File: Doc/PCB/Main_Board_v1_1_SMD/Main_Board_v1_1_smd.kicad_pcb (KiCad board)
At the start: 2 copper layers, 180 x 98 mm, 138 parts, among them J1 TE_3.5mm_Screwless_P2, J10 BPM, J11 UART, J12 I2C Interface LCD_C, J13 BUZZER_C, J16 IP, J17 -, J19 EP, J2 TE_3.5mm_Screwless_P2, J20 +, J21 VOL_MIN, J22 VOL, J23 VOL_MAX, J24 Conn_01x08, J25 POWEROFF, J26 PMAX, J3 UART_M, J4 Conn_01x08, J5 BUZZER, J6 I2C Interface LCD_M, J7 TE_3.5mm_Screwless_P2, J8 SV2, J9 SV3, Q1 FDT1600N10ALZ, Q2 FDT1600N10ALZ, Q3 FDT1600N10ALZ, Q4 BSR19A, Q5 BSR19A, SW1 MUTE, SW10 BREATH, SW11 EP, SW12 +, SW2 HIST, SW3 VOL_MIN, SW4 VOL, SW5 PBM, SW6 IP, SW7 -, SW8 VOL_MAX, SW9 PMAX, U1 LM358, U2 LM78M05_TO252, U3 XPRESS-40, U4 LM78M05_TO252, U5 XPRESS-40, U6 LCD, U7 LCD

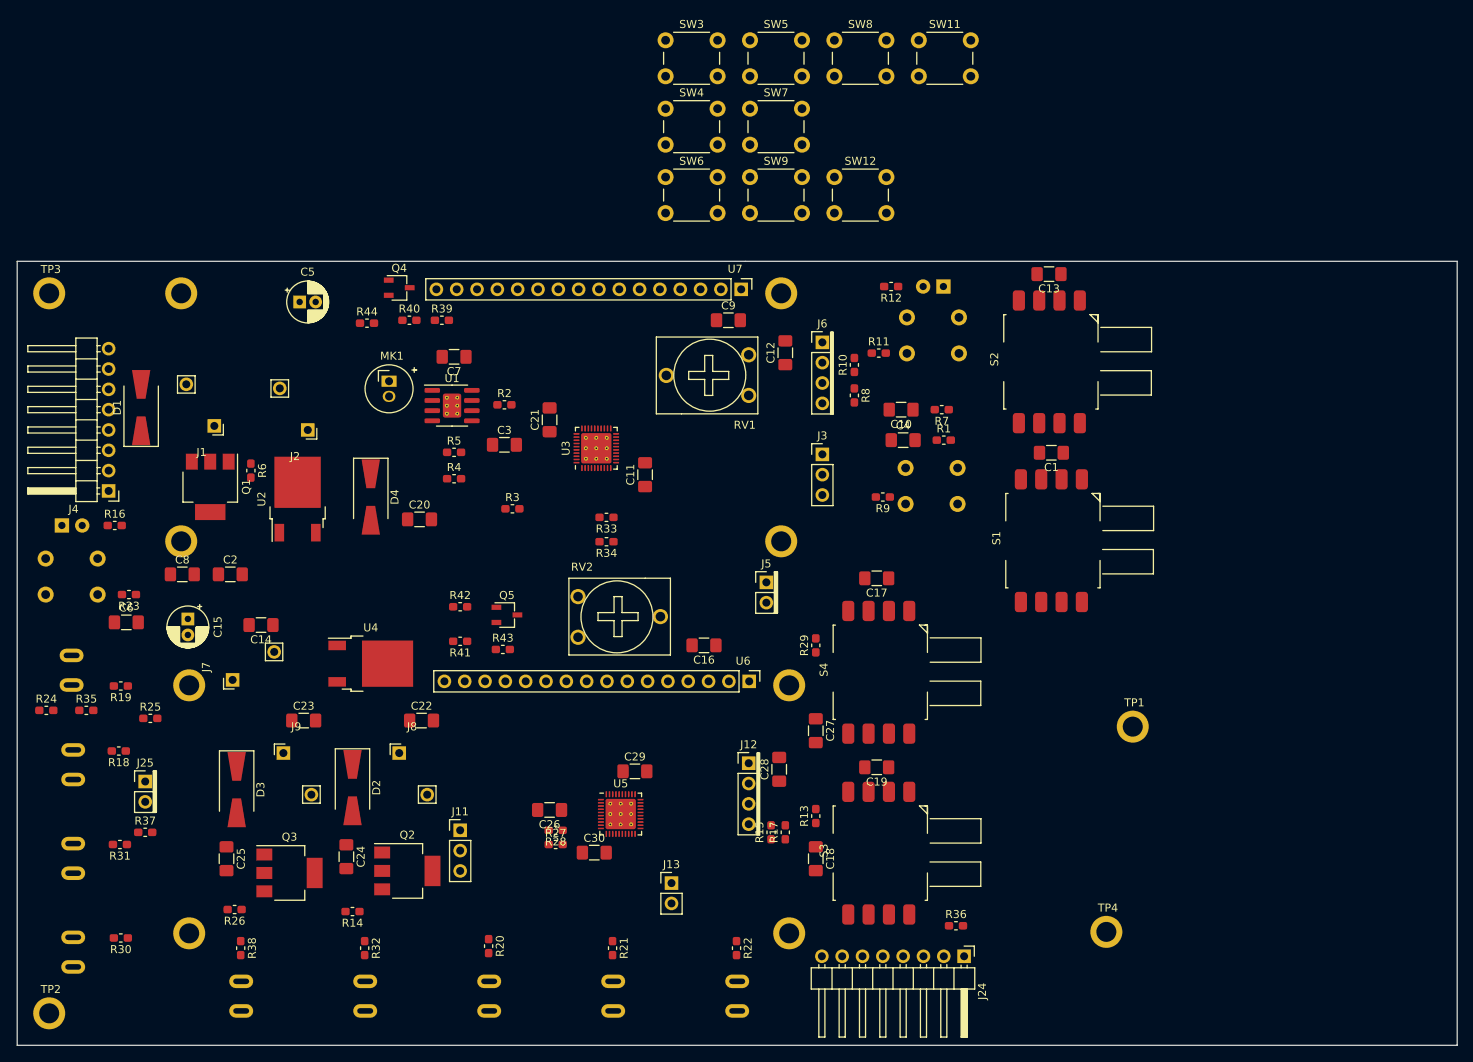
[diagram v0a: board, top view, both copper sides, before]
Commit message: First tests with artificial lung. 70 cases. New PCB THT fixing mounting issues
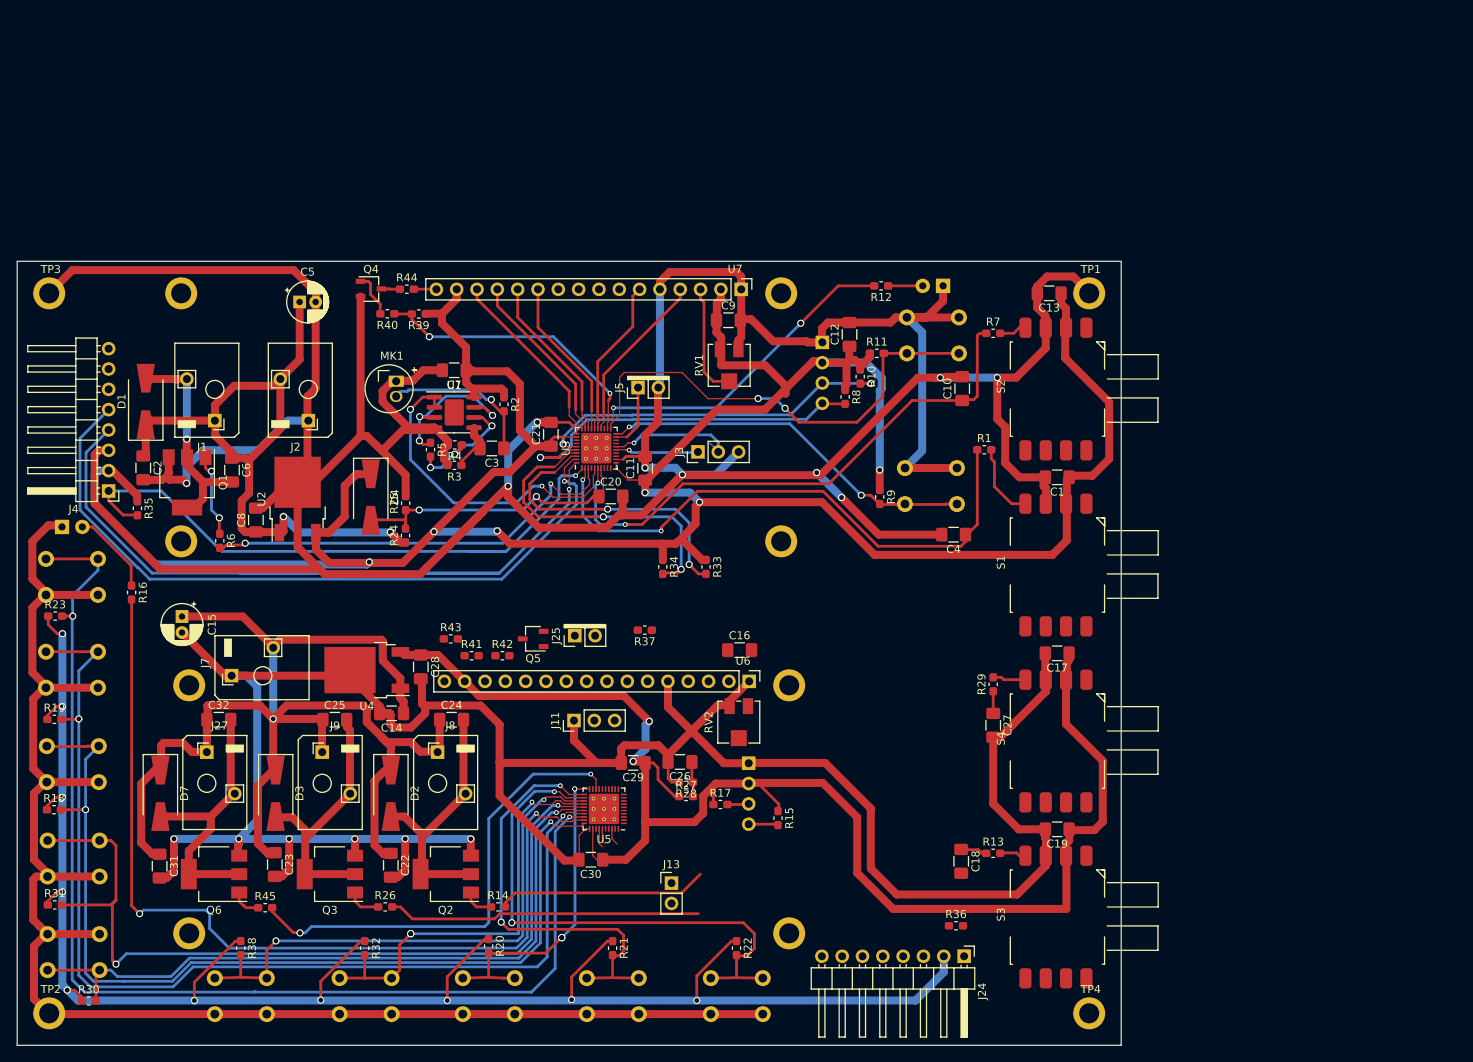
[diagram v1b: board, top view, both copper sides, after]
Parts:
- removed J10: BPM, Ventilator:PushButton
- removed J16: IP, Ventilator:PushButton
- removed J17: -, Ventilator:PushButton
- removed J19: EP, Ventilator:PushButton
- removed J20: +, Ventilator:PushButton
- removed J21: VOL_MIN, Ventilator:PushButton
- removed J22: VOL, Ventilator:PushButton
- removed J23: VOL_MAX, Ventilator:PushButton
- removed J26: PMAX, Ventilator:PushButton
- added C31: 1uF, Capacitor_SMD:C_1206_3216Metric_Pad1.42x1.75mm_HandSolder, F.Cu at (45.2, 108.5)
- added C32: 1uF, Capacitor_SMD:C_1206_3216Metric_Pad1.42x1.75mm_HandSolder, F.Cu at (52.6, 90.2)
- added D7: 1A - 100V, Diode_SMD:D_SMA-SMB_Universal_Handsoldering, F.Cu at (45.3, 99.4)
- added J27: SV2, Ventilator:PinHeader_1x02_Screwless_3.5mm, F.Cu at (51.1, 94.2)
- added Q6: FDT1600N10ALZ, Package_TO_SOT_SMD:SOT-223-3_TabPin2, F.Cu at (52.0, 109.5)
- added R45: 1k, Resistor_SMD:R_0603_1608Metric_Pad1.05x0.95mm_HandSolder, F.Cu at (58.4, 113.7)
- D5: value LED -> ALARM
- J12, J6, SW11, SW12, SW3, SW4, SW6, SW7, SW8, SW9: moved to B.Cu
- R43, R44: value 4.7 -> 1k
- RV1, RV2: value 1K -> 5K; footprint Ventilator:Potentiometer_409HA -> Potentiometer_SMD:Potentiometer_Vishay_TS53YJ_Vertical
- SW5: value PBM -> BPM; moved to B.Cu
- U1: footprint Package_SO:SOIC-8-1EP_3.9x4.9mm_P1.27mm_EP2.29x3mm_ThermalVias -> Package_SO:SOIC-8-1EP_3.9x4.9mm_P1.27mm_EP2.41x3.3mm
- moved SW3 139.6 mm to (31.2, 121.5)
- moved SW8 135.8 mm to (37.7, 105.3), turned to 180 degrees
- moved SW11 122.3 mm to (105.1, 122.5), turned to 180 degrees
- moved SW5 117.2 mm to (120.6, 122.5), turned to 180 degrees
- moved SW9 116.9 mm to (58.6, 122.5), turned to 180 degrees
- moved SW4 113.9 mm to (74.2, 122.5), turned to 180 degrees
- moved SW7 113.9 mm to (37.6, 93.5), turned to 180 degrees
- moved SW12 109.5 mm to (37.5, 81.7), turned to 180 degrees
- moved SW6 101.9 mm to (89.6, 122.5), turned to 180 degrees
- moved R37 67.4 mm to (105.8, 79.0), turned to 180 degrees
- moved J25 56.7 mm to (97.1, 79.7), turned to 90 degrees
- moved TP1 54.4 mm to (161.4, 36.9)
- moved R24 49.9 mm to (75.9, 67.1), turned to 90 degrees
- moved C28 46.6 mm to (77.8, 83.6), turned to 270 degrees
- moved R25 41.7 mm to (75.9, 63.1), turned to 90 degrees
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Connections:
- net /Controller/BPM renamed Net-(R22-Pad2)
- net /Controller/BREATH renamed Net-(R23-Pad2)
- net /Controller/EP renamed Net-(R21-Pad2)
- net /Controller/IP renamed Net-(R20-Pad2)
- net /Controller/MINUS renamed Net-(R18-Pad2)
- net /Controller/PLUS renamed Net-(R19-Pad2)
- net /Controller/PMAX renamed Net-(R38-Pad2)
- net /Controller/VOL renamed Net-(R32-Pad2)
- net /Controller/VOL_MAX renamed Net-(R31-Pad2)
- net /Controller/VOL_MIN renamed Net-(R30-Pad2)
- Q5 pad 1: Net-(Q5-Pad1) -> GND
- Q5 pad 2: GND -> Net-(Q5-Pad2)
- R42 pad 2: Net-(Q5-Pad1) -> Net-(Q5-Pad2)
- RV2 pad 1: +5V_C -> GND
- RV2 pad 3: GND -> +5V_C
- SW10 pad 2: Net-(SW10-Pad2) -> GND
- U5 pad 18: (no net) -> /Controller/SV4
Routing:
- net GND: track 0.00 -> 1038.6 mm, vias 0 -> 15
- net +5V_C: track 0.00 -> 404.2 mm, vias 0 -> 12
- net +5V_M: track 0.00 -> 371.3 mm, vias 0 -> 6
- net +12V_C: track 0.00 -> 155.7 mm, vias 0 -> 1
- net Net-(R23-Pad2): track 0.00 -> 145.7 mm, vias 0 -> 2
- net Net-(R19-Pad2): track 0.00 -> 132.3 mm, vias 0 -> 2
- net Net-(R18-Pad2): track 0.00 -> 118.2 mm, vias 0 -> 2
- net /Monitor/ICSPDAT_M: track 0.00 -> 116.1 mm, vias 0 -> 1
- net Net-(R16-Pad2): track 0.00 -> 114.4 mm, vias 0 -> 2
- net Net-(R31-Pad2): track 0.00 -> 106.2 mm, vias 0 -> 2
- net /Monitor/ICSPCLK_M: track 0.00 -> 91.2 mm, vias 0 -> 1
- net Net-(R30-Pad2): track 0.00 -> 88.4 mm, vias 0 -> 1
- net +12V_M: track 0.00 -> 87.1 mm, vias 0 -> 2
- net /Monitor/nMCLR_M: track 0.00 -> 78.3 mm, vias 0 -> 1
- net /Monitor/PTR2: track 0.00 -> 72.2 mm, vias 0 -> 2
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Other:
- board size 180 x 98 mm -> 138 x 98 mm
- net class Default: clearance 0.4 -> 0.2
- net class Power + added: clearance 0.4, trace_width 2, via_dia 0.9, via_drill 0.6
- net class fanout added: clearance 0.2, trace_width 0.15, via_dia 0.6, via_drill 0.35
- rule trace_clearance: 0.4 -> 0.2
- rule trace_min: 0.2 -> 0.1
- rule via_min_size: 0.4 -> 0.35

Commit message: Update THT board reducing to class 3
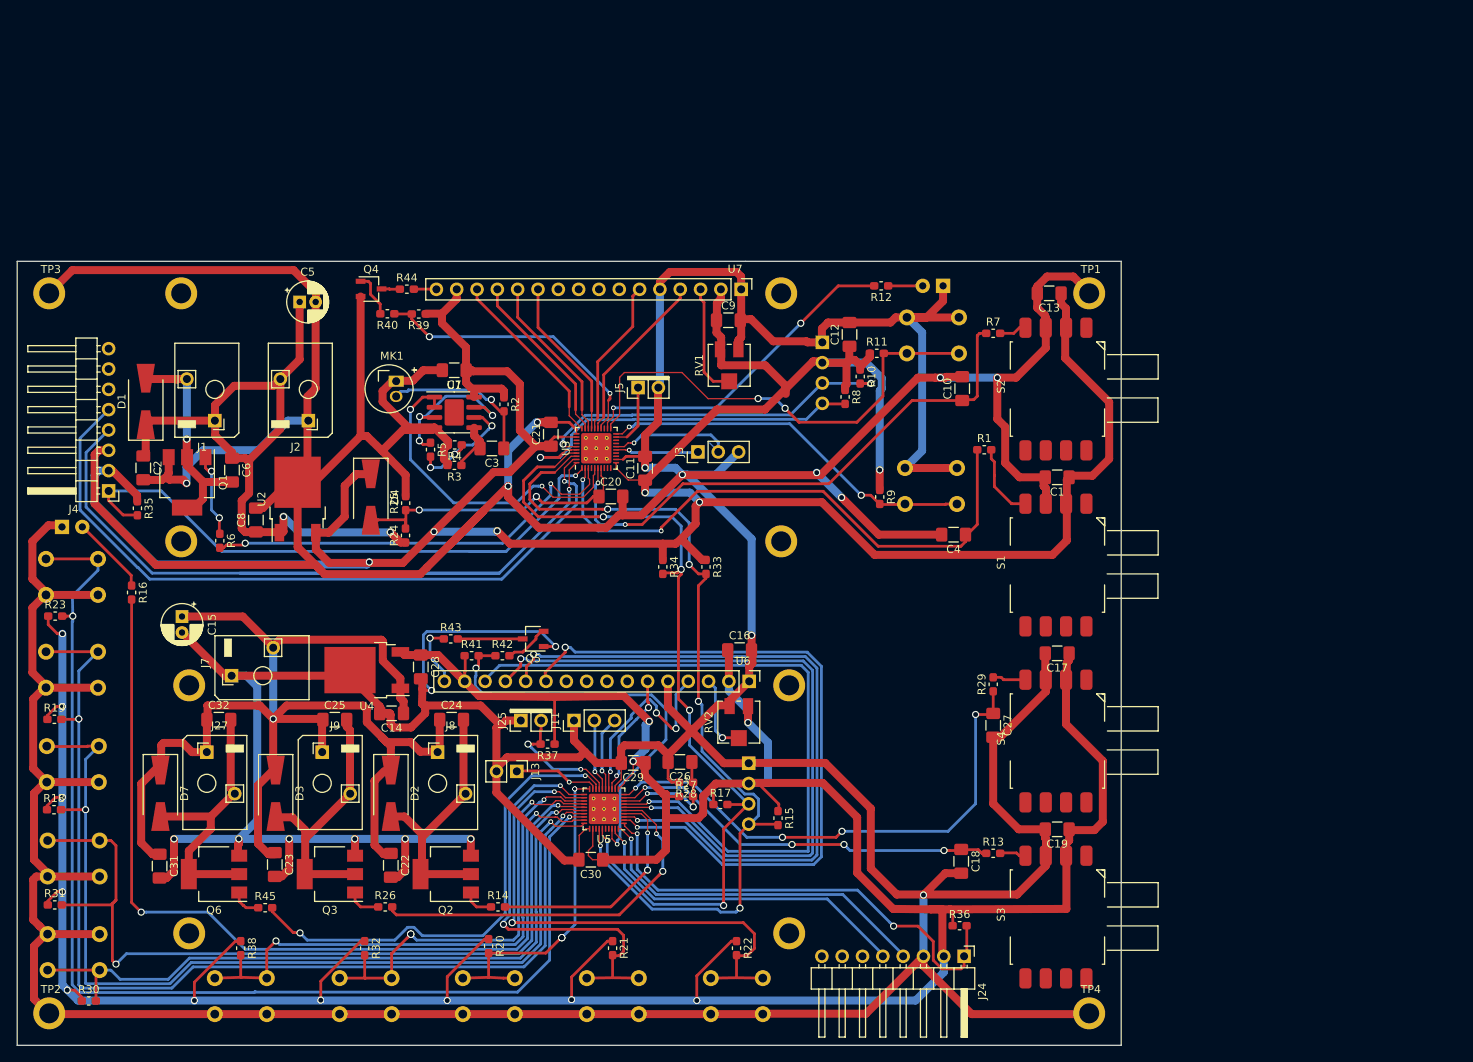
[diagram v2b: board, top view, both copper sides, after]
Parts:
- moved J13 23.9 mm to (89.8, 96.6), turned to 270 degrees
- moved R37 18.7 mm to (93.7, 93.2)
- moved J25 12.6 mm to (90.3, 90.3)
- moved R36 0.45 mm to (145.2, 115.9)
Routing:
- net GND: track 1038.6 -> 1161.6 mm, vias 15 -> 19
- net /Controller/LD5: track 0.00 -> 90.0 mm, vias 0 -> 2
- net /Controller/LD6: track 0.00 -> 89.9 mm, vias 0 -> 2
- net /Controller/LD7: track 0.00 -> 89.7 mm, vias 0 -> 1
- net /Controller/LD4: track 0.00 -> 89.6 mm, vias 0 -> 2
- net SCL: track 44.2 -> 112.8 mm, vias 2 -> 5
- net SDA: track 44.1 -> 110.1 mm, vias 2 -> 5
- net /Controller/PR_AUX: track 2.55 -> 65.0 mm, vias 0 -> 4
- net /Controller/nMCLR_C: track 0.00 -> 59.6 mm, vias 0 -> 2
- net /Controller/LLED: track 2.19 -> 52.8 mm, vias 0 -> 2
- net /Controller/PR_MAIN: track 3.31 -> 49.3 mm, vias 0 -> 4
- net /Controller/ICSPDAT_C: track 0.00 -> 44.4 mm, vias 0 -> 1
- net +5V_C: track 404.2 -> 446.7 mm, vias 12 -> 13
- net /Controller/ICSPCLK_C: track 0.00 -> 42.4 mm, vias 0 -> 1
- net /Controller/LDRS: track 0.00 -> 25.2 mm, vias 0 -> 3
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
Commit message: New SMD PCB
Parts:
- J1: value TE_3.5mm_Screwless_P2 -> SV1
- J11: value UART -> UART_C
- J2: value TE_3.5mm_Screwless_P2 -> 12V
- J5: value BUZZER -> BUZZER_M
- U3, U5: footprint Package_DFN_QFN:UQFN-40-1EP_5x5mm_P0.4mm_EP3.8x3.8mm_ThermalVias -> Package_DFN_QFN:UQFN-40-1EP_5x5mm_P0.4mm_EP3.8x3.8mm
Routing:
- net /Monitor/ICSPDAT_M: track 116.1 -> 85.1 mm
- net +5V_C: track 446.7 -> 459.3 mm
- net GND: track 1161.6 -> 1174.1 mm
- net Net-(R21-Pad2): track 54.2 -> 59.4 mm
- net /Controller/LLED: track 52.8 -> 57.3 mm
- net +5V_M: track 371.3 -> 375.3 mm
- net /Monitor/ICSPCLK_M: track 91.2 -> 94.2 mm
- net /Controller/SV2: track 29.3 -> 32.1 mm
- net /Monitor/TX: track 16.6 -> 13.8 mm
- net /Controller/SV4: track 61.0 -> 63.7 mm
- net /Controller/LD4: track 89.6 -> 92.0 mm
- net /Controller/SV3: track 47.7 -> 50.1 mm
- net /Monitor/ALARM_MUTE: track 58.9 -> 60.9 mm
- net Net-(R22-Pad2): track 68.7 -> 70.7 mm
- net Net-(R32-Pad2): track 54.0 -> 55.8 mm, vias 3 -> 2
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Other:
- net class Default: via_dia 0.9 -> 1
- net class Power: clearance 0.4 -> 0.2; via_dia 0.9 -> 1
- net class Power + removed
- net class fanout removed
- rule trace_min: 0.1 -> 0.2
- rule via_min_size: 0.35 -> 0.6
- board text added: "+"
- board text added: "12V"
- board text added: "Flow"
- board text added: "PressExt"
- board text added: "PressInt"
- board text added: "SV1"
- board text added: "SV2"
- board text added: "SV3"
- board text added: "SV4"
